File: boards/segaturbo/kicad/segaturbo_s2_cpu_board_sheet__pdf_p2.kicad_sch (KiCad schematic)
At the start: 23 parts, among them CN1 Conn_02x25, CN2 Conn_02x25, CN3 Conn_01x12, IC100 74LS174, IC101 MB8128, IC102 74LS157, IC103 2764, IC110 74LS166, IC111 2716, IC112 74LS273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

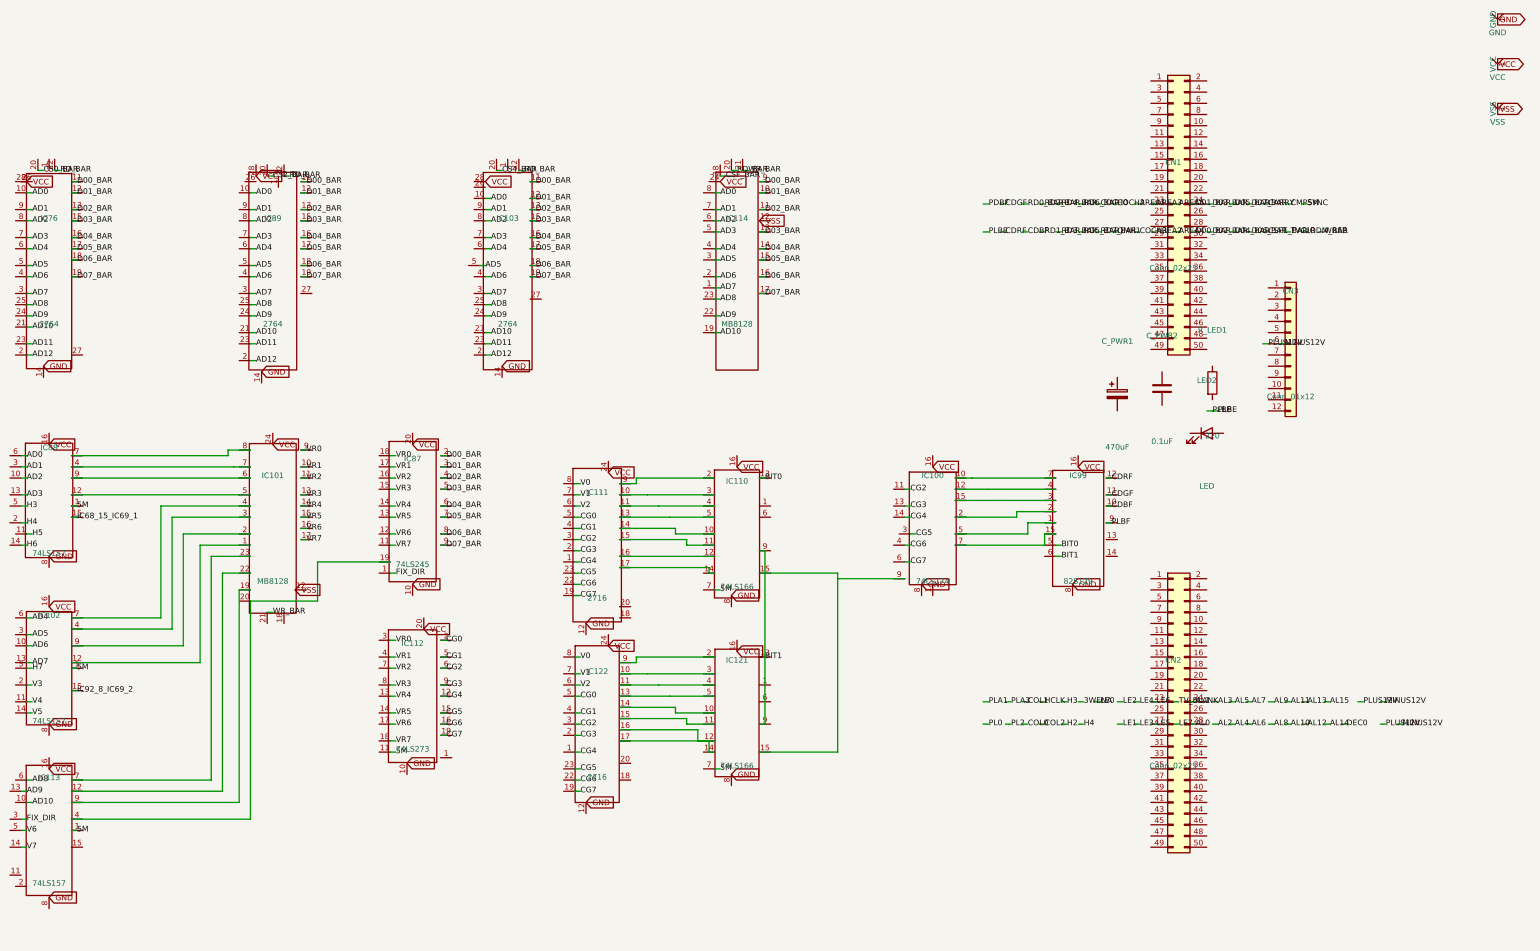
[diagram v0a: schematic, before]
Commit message: Fix KiCad pin-aligned generated symbols
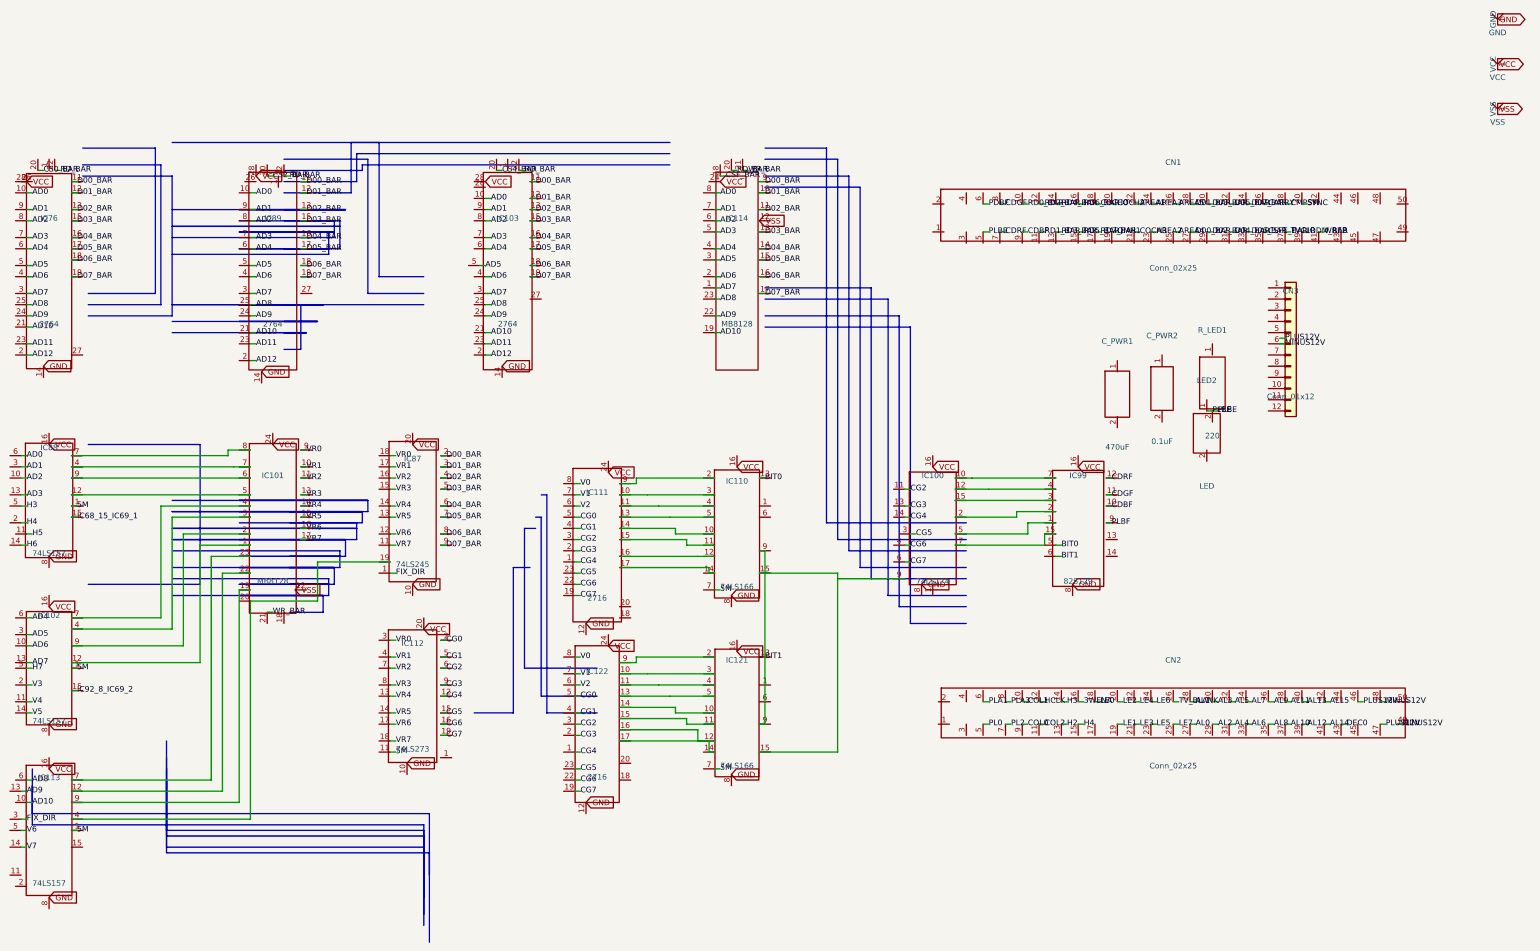
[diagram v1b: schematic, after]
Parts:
- CN1: symbol Connector_Generic:Conn_02x25_Odd_Even -> user:_chip_CN1
- CN2: symbol Connector_Generic:Conn_02x25_Odd_Even -> user:_chip_CN2
- C_PWR1: symbol Device:C_Polarized -> user:_chip_C_PWR1
- C_PWR2: symbol Device:C -> user:_chip_C_PWR2
- LED2: symbol Device:LED -> user:_chip_LED2
- R_LED1: symbol Device:R -> user:_chip_R_LED1
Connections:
- net 3WENA: now also CN2.16
- net 5M: now also CN1.40
- net AL0: now also CN2.27
- net AL1: now also CN2.28
- net AL10: now also CN2.37
- net AL11: now also CN2.38
- net AL12: now also CN2.39
- net AL13: now also CN2.40
- net AL14: now also CN2.41
- net AL15: now also CN2.42
- net AL2: now also CN2.29
- net AL3: now also CN2.30
- net AL4: now also CN2.31
- net AL5: now also CN2.32
- net AL6: now also CN2.33
- net AL7: now also CN2.34
- net AL8: now also CN2.35
- net AL9: now also CN2.36
- net AREA1: now also CN1.22
- net AREA2: now also CN1.23
- net AREA3: now also CN1.24; no longer CN1.23 (Pin_23)
- net AREA4: now also CN1.25
- net AREA5: now also CN1.26
- net CARRY: now also CN1.36
- net CDBF: now also CN1.9
- net CDGF: now also CN1.8
- net CDRF: now also CN1.7
- net CMPSYNC: now also CN1.38
- net COCH0: now also CN1.18
- net COCH2: now also CN1.20
- net COCH3: now also CN1.21
- net COL0: now also CN2.9
- net COL1: now also CN2.10
- net COL2: now also CN2.11
- net CSFE_BAR: now also CN1.35
- net D00_BAR: now also CN1.27
- net D01_BAR: now also CN1.28
- net D02_BAR: now also CN1.29
- net D03_BAR: now also CN1.30; no longer CN1.24 (Pin_24)
- net D04_BAR: now also CN1.31
- net D05_BAR: now also CN1.32
- net D06_BAR: now also CN1.33
- net D07_BAR: now also CN1.34
- net DEC0: now also CN2.43
- net H2: now also CN2.13
- net H3: now also CN2.14
- net H4: now also CN2.15
- net HCLK: now also CN2.12
- net IODM_BAR: now also CN1.39
- net LE0: now also CN2.18
- net LE1: now also CN2.19
- net LE2: now also CN2.20
- net LE3: now also CN2.21
- net LE4: now also CN2.22
- net LE5: now also CN2.23; no longer CN2.27 (Pin_27)
- net LE6: now also CN2.24; no longer CN2.23 (Pin_23)
- net LE7: now also CN2.25
- net MINUS12V: now also CN2.48, CN2.49
- net PDBF: now also CN1.6
- net PL0: now also CN2.5
- net PL2: now also CN2.7
- net PLA1: now also CN2.6
- net PLA3: now also CN2.8
- net PLBE: now also CN1.5, LED2.1 (+), R_LED1.2
- net PLUS12V: now also CN2.46, CN2.47; no longer CN3.6 (Pin_6)
- net QMH1: now also CN1.19
- net RD0_BAR: now also CN1.10
- net RD1_BAR: now also CN1.11
- net RD2_BAR: now also CN1.12
- net RD3_BAR: now also CN1.13
- net RD4_BAR: now also CN1.14
- net RD5_BAR: now also CN1.15
- net RD6_BAR: now also CN1.16
- net RD7_BAR: now also CN1.17
- net TVCLR: now also CN1.37
- net TV_BLANK: now also CN2.26
- net WREB: now also CN1.41
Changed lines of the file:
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@@
   )
   (symbol
-    (lib_id "Connector_Generic:Conn_02x25_Odd_Even")
+    (lib_id "user:_chip_CN1")
     (at 326.39 62.23 0)
     (unit 1)
@@
   )
   (symbol
-    (lib_id "Connector_Generic:Conn_02x25_Odd_Even")
+    (lib_id "user:_chip_CN2")
     (at 326.39 175.26 0)
     (unit 1)
@@
   )
   (symbol
-    (lib_id "Device:C_Polarized")
+    (lib_id "user:_chip_C_PWR1")
     (at 313.69 102.87 0)
     (unit 1)
@@
   )
   (symbol
-    (lib_id "Device:C")
+    (lib_id "user:_chip_C_PWR2")
     (at 323.85 101.6 0)
     (unit 1)
@@
   )
   (symbol
-    (lib_id "Device:LED")
+    (lib_id "user:_chip_LED2")
     (at 334.01 111.76 0)
     (unit 1)
@@
   )
   (symbol
-    (lib_id "Device:R")
+    (lib_id "user:_chip_R_LED1")
     (at 335.28 100.33 0)
     (unit 1)
@@
     (stroke (width 0) (type default))
   )
-  (wire (pts (xy 346.71 91.44) (xy 347.98 91.44))
+  (wire (pts (xy 350.52 90.17) (xy 351.79 90.17))
     (stroke (width 0) (type default))
   )
@@
     (stroke (width 0) (type default))
   )
+  (polyline (pts (xy 156.21 82.55) (xy 128.27 82.55) (xy 128.27 92.71) (xy 124.46 92.71))
+    (stroke (width 0.1524) (type default))
+    (fill (type none))
+  )
+  (polyline (pts (xy 114.3 88.9) (xy 129.54 88.9) (xy 129.54 88.9) (xy 124.46 88.9) (xy 129.54 88.9) (xy 129.54 88.9) (xy 99.06 88.9))
+    (stroke (width 0.1524) (type default))
+    (fill (type none))
+  )
+  (polyline (pts (xy 124.46 86.36) (xy 132.08 86.36) (xy 132.08 86.36) (xy 114.3 86.36) (xy 132.08 86.36) (xy 132.08 86.36) (xy 99.06 86.36))
+    (stroke (width 0.1524) (type default))
+    (fill (type none))
+  )
+  (polyline (pts (xy 124.46 82.55) (xy 133.35 82.55) (xy 133.35 82.55) (xy 99.06 82.55) (xy 133.35 82.55) (xy 133.35 82.55) (xy 114.3 82.55))
+    (stroke (width 0.1524) (type default))
+    (fill (type none))
+  )
+  (polyline (pts (xy 124.46 66.04) (xy 134.62 66.04) (xy 134.62 69.85) (xy 114.3 69.85) (xy 134.62 69.85) (xy 134.62 71.12) (xy 99.06 71.12))
+    (stroke (width 0.1524) (type default))
+    (fill (type none))
+  )
+  (polyline (pts (xy 124.46 63.5) (xy 135.89 63.5) (xy 135.89 66.04) (xy 114.3 66.04) (xy 135.89 66.04) (xy 135.89 67.31) (xy 99.06 67.31))
+    (stroke (width 0.1524) (type default))
+    (fill (type none))
+  )
+  (polyline (pts (xy 114.3 63.5) (xy 137.16 63.5) (xy 137.16 64.77) (xy 99.06 64.77) (xy 137.16 64.77) (xy 137.16 69.85) (xy 124.46 69.85))
+    (stroke (width 0.1524) (type default))
+    (fill (type none))
+  )
+  (polyline (pts (xy 99.06 60.96) (xy 138.43 60.96) (xy 138.43 60.96) (xy 114.3 60.96) (xy 138.43 60.96) (xy 124.46 60.96))
+    (stroke (width 0.1524) (type default))
+    (fill (type none))
+  )
+  (polyline (pts (xy 212.09 45.72) (xy 139.7 45.72) (xy 139.7 57.15) (xy 124.46 57.15))
+    (stroke (width 0.1524) (type default))
+    (fill (type none))
+  )
+  (polyline (pts (xy 212.09 48.26) (xy 140.97 48.26) (xy 140.97 54.61) (xy 124.46 54.61))
+    (stroke (width 0.1524) (type default))
+    (fill (type none))
+  )
+  (polyline (pts (xy 212.09 50.8) (xy 142.24 50.8) (xy 142.24 52.07) (xy 124.46 52.07))
+    (stroke (width 0.1524) (type default))
+    (fill (type none))
+  )
+  (polyline (pts (xy 124.46 49.53) (xy 143.51 49.53) (xy 143.51 80.01) (xy 156.21 80.01))
+    (stroke (width 0.1524) (type default))
+    (fill (type none))
+  )
+  (polyline (pts (xy 99.06 45.72) (xy 146.05 45.72) (xy 146.05 76.2) (xy 156.21 76.2))
+    (stroke (width 0.1524) (type default))
+    (fill (type none))
+  )
+  (polyline (pts (xy 99.06 148.59) (xy 133.35 148.59) (xy 133.35 148.59) (xy 114.3 148.59) (xy 133.35 148.59) (xy 133.35 152.4) (xy 125.73 152.4))
+    (stroke (width 0.1524) (type default))
+    (fill (type none))
+  )
+  (polyline (pts (xy 99.06 144.78) (xy 134.62 144.78) (xy 134.62 146.05) (xy 114.3 146.05) (xy 134.62 146.05) (xy 134.62 148.59) (xy 125.73 148.59))
+    (stroke (width 0.1524) (type default))
+    (fill (type none))
+  )
+  (polyline (pts (xy 99.06 142.24) (xy 135.89 142.24) (xy 135.89 142.24) (xy 114.3 142.24) (xy 135.89 142.24) (xy 135.89 146.05) (xy 125.73 146.05))
+    (stroke (width 0.1524) (type default))
+    (fill (type none))
+  )
+  (polyline (pts (xy 99.06 138.43) (xy 137.16 138.43) (xy 137.16 139.7) (xy 114.3 139.7) (xy 137.16 139.7) (xy 137.16 142.24) (xy 125.73 142.24))
+    (stroke (width 0.1524) (type default))
+    (fill (type none))
+  )
+  (polyline (pts (xy 114.3 135.89) (xy 138.43 135.89) (xy 138.43 135.89) (xy 99.06 135.89) (xy 138.43 135.89) (xy 138.43 139.7) (xy 125.73 139.7))
+    (stroke (width 0.1524) (type default))
+    (fill (type none))
+  )
+  (polyline (pts (xy 114.3 132.08) (xy 140.97 132.08) (xy 140.97 133.35) (xy 99.06 133.35) (xy 140.97 133.35) (xy 140.97 135.89) (xy 125.73 135.89))
+    (stroke (width 0.1524) (type default))
+    (fill (type none))
+  )
+  (polyline (pts (xy 114.3 129.54) (xy 142.24 129.54) (xy 142.24 129.54) (xy 99.06 129.54) (xy 142.24 129.54) (xy 142.24 132.08) (xy 125.73 132.08))
+    (stroke (width 0.1524) (type default))
+    (fill (type none))
+  )
+  (polyline (pts (xy 99.06 127) (xy 143.51 127) (xy 143.51 127) (xy 114.3 127) (xy 143.51 127) (xy 143.51 129.54) (xy 125.73 129.54))
+    (stroke (width 0.1524) (type default))
+    (fill (type none))
+  )
+  (polyline (pts (xy 67.31 191.77) (xy 67.31 200.66) (xy 156.21 200.66) (xy 156.21 214.63))
+    (stroke (width 0.1524) (type default))
+    (fill (type none))
+  )
+  (polyline (pts (xy 97.79 181.61) (xy 97.79 201.93) (xy 156.21 201.93) (xy 156.21 217.17))
+    (stroke (width 0.1524) (type default))
+    (fill (type none))
+  )
+  (polyline (pts (xy 97.79 185.42) (xy 97.79 203.2) (xy 156.21 203.2) (xy 156.21 220.98))
+    (stroke (width 0.1524) (type default))
+    (fill (type none))
+  )
+  (polyline (pts (xy 97.79 187.96) (xy 97.79 205.74) (xy 156.21 205.74) (xy 156.21 223.52))
+    (stroke (width 0.1524) (type default))
+    (fill (type none))
+  )
+  (polyline (pts (xy 97.79 190.5) (xy 97.79 207.01) (xy 157.48 207.01) (xy 157.48 227.33))
+    (stroke (width 0.1524) (type default))
+    (fill (type none))
+  )
+  (polyline (pts (xy 180.34 142.24) (xy 176.53 142.24) (xy 176.53 175.26) (xy 167.64 175.26))
+    (stroke (width 0.1524) (type default))
+    (fill (type none))
+  )
+  (polyline (pts (xy 181.61 133.35) (xy 179.07 133.35) (xy 179.07 165.1) (xy 195.58 165.1))
+    (stroke (width 0.1524) (type default))
+    (fill (type none))
+  )
+  (polyline (pts (xy 80.01 114.3) (xy 105.41 114.3) (xy 105.41 146.05) (xy 80.01 146.05))
+    (stroke (width 0.1524) (type default))
+    (fill (type none))
+  )
+  (polyline (pts (xy 181.61 130.81) (xy 182.88 130.81) (xy 182.88 171.45) (xy 195.58 171.45))
+    (stroke (width 0.1524) (type default))
+    (fill (type none))
+  )
+  (polyline (pts (xy 182.88 125.73) (xy 184.15 125.73) (xy 184.15 175.26) (xy 195.58 175.26))
+    (stroke (width 0.1524) (type default))
+    (fill (type none))
+  )
+  (polyline (pts (xy 233.68 49.53) (xy 250.19 49.53) (xy 250.19 135.89) (xy 279.4 135.89))
+    (stroke (width 0.1524) (type default))
+    (fill (type none))
+  )
+  (polyline (pts (xy 233.68 55.88) (xy 255.27 55.88) (xy 255.27 142.24) (xy 279.4 142.24))
+    (stroke (width 0.1524) (type default))
+    (fill (type none))
+  )
+  (polyline (pts (xy 233.68 81.28) (xy 261.62 81.28) (xy 261.62 148.59) (xy 279.4 148.59))
+    (stroke (width 0.1524) (type default))
+    (fill (type none))
+  )
+  (polyline (pts (xy 233.68 87.63) (xy 266.7 87.63) (xy 266.7 154.94) (xy 279.4 154.94))
+    (stroke (width 0.1524) (type default))
+    (fill (type none))
+  )
+  (polyline (pts (xy 67.31 187.96) (xy 67.31 198.12) (xy 157.48 198.12) (xy 157.48 212.09))
+    (stroke (width 0.1524) (type default))
+    (fill (type none))
+  )
+  (polyline (pts (xy 233.68 46.99) (xy 247.65 46.99) (xy 247.65 132.08) (xy 279.4 132.08))
+    (stroke (width 0.1524) (type default))
+    (fill (type none))
+  )
+  (polyline (pts (xy 233.68 53.34) (xy 252.73 53.34) (xy 252.73 138.43) (xy 279.4 138.43))
+    (stroke (width 0.1524) (type default))
+    (fill (type none))
+  )
+  (polyline (pts (xy 233.68 78.74) (xy 257.81 78.74) (xy 257.81 144.78) (xy 279.4 144.78))
+    (stroke (width 0.1524) (type default))
+    (fill (type none))
+  )
+  (polyline (pts (xy 233.68 85.09) (xy 264.16 85.09) (xy 264.16 151.13) (xy 279.4 151.13))
+    (stroke (width 0.1524) (type default))
+    (fill (type none))
+  )
+  (polyline (pts (xy 78.74 46.99) (xy 95.25 46.99) (xy 95.25 80.01) (xy 80.01 80.01))
+    (stroke (width 0.1524) (type default))
+    (fill (type none))
+  )
+  (polyline (pts (xy 78.74 50.8) (xy 96.52 50.8) (xy 96.52 82.55) (xy 80.01 82.55))
+    (stroke (width 0.1524) (type default))
+    (fill (type none))
+  )
+  (polyline (pts (xy 78.74 53.34) (xy 99.06 53.34) (xy 99.06 85.09) (xy 80.01 85.09))
+    (stroke (width 0.1524) (type default))
+    (fill (type none))
+  )
   (global_label "GND" (shape output) (at 400.05 17.78 0)
     (effects (font (size 1.27 1.27)) (justify left))
@@
     (effects (font (size 1.27 1.27)) (justify left))
   )
-  (label "PLUS12V" (at 347.98 91.44 0)
-    (effects (font (size 1.27 1.27)) (justify left))
-  )
+  (label "PLUS12V" (at 351.79 90.17 0)
+    (effects (font (size 1.27 1.27)) (justify left))
+  )
